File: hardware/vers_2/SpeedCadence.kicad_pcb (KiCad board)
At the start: 2 copper layers, 2 parts, among them IC1 AH1912-W-7, U2 STM32F103C8Tx

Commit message: PCB design complete
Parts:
- removed IC1: AH1912-W-7, Package_TO_SOT_SMD:SOT-23-3
- added C1: 100n, Capacitor_SMD:C_0805_2012Metric, F.Cu at (177.7, 107.2)
- added C10: 4.7n, Capacitor_SMD:C_0805_2012Metric, F.Cu at (157.8, 90.3)
- added C2: 100n, Capacitor_SMD:C_0805_2012Metric, F.Cu at (165.5, 104.2)
- added C3: 100n, Capacitor_SMD:C_0805_2012Metric, F.Cu at (167.7, 96.0)
- added C4: 100n, Capacitor_SMD:C_0805_2012Metric, F.Cu at (181.0, 96.3)
- added C5: 10u, Capacitor_SMD:C_0805_2012Metric, F.Cu at (174.6, 108.0)
- added C6: 100n, Capacitor_SMD:C_0805_2012Metric, F.Cu at (181.0, 98.6)
- added C7: 100n, Capacitor_SMD:C_0805_2012Metric, F.Cu at (165.5, 100.3)
- added C8: 1u, Capacitor_SMD:C_0805_2012Metric, F.Cu at (156.3, 103.2)
- added C9: 1u, Capacitor_SMD:C_0805_2012Metric, F.Cu at (163.2, 103.2)
- added D1: PTVS5V0Z1USK, Diode_SMD:Nexperia_DSN1608-2_1.6x0.8mm, F.Cu at (153.9, 111.1)
- added D2: D_Schottky, Diode_SMD:D_SOD-123, F.Cu at (156.3, 109.1)
- added D3: D_Schottky, Diode_SMD:D_SOD-123, F.Cu at (156.7, 98.3)
- added F1: Polyfuse, Fuse:Fuse_1206_3216Metric, F.Cu at (150.6, 111.1)
- added H1: MountingHole, MountingHole:MountingHole_2.2mm_M2, F.Cu at (187.4, 114.6)
- added H2: MountingHole, MountingHole:MountingHole_2.2mm_M2, F.Cu at (146.9, 114.6)
- added H3: MountingHole, MountingHole:MountingHole_2.2mm_M2, F.Cu at (187.4, 89.2)
- added H4: MountingHole, MountingHole:MountingHole_2.2mm_M2, F.Cu at (146.9, 89.2)
- added J1: Conn_ST_STDC14, Connector_PinHeader_1.27mm:PinHeader_2x07_P1.27mm_Vertical_SMD, F.Cu at (163.6, 111.6)
- added J2: USB_C_Receptacle_USB2.0_16P, Connector_USB:USB_C_Receptacle_HRO_TYPE-C-31-M-12, F.Cu at (149.4, 104.2)
- added J3: Conn_01x03_Pin, Connector_JST:JST_XH_B3B-XH-A_1x03_P2.50mm_Vertical, F.Cu at (176.1, 90.8)
- added J4: Conn_01x02_Pin, Connector_JST:JST_XH_B2B-XH-A_1x02_P2.50mm_Vertical, F.Cu at (167.4, 90.7)
- added J5: Conn_01x04_Pin, Connector_JST:JST_XH_B4B-XH-A_1x04_P2.50mm_Vertical, F.Cu at (173.1, 112.0)
- added J6: Conn_01x02_Pin, Connector_JST:JST_PH_B2B-PH-K_1x02_P2.00mm_Vertical, F.Cu at (147.4, 96.3)
- added R1: 5.1k, Resistor_SMD:R_0805_2012Metric, F.Cu at (153.1, 97.7)
- added R2: 5.1k, Resistor_SMD:R_0805_2012Metric, F.Cu at (153.0, 92.8)
- added R3: 60, Resistor_SMD:R_0805_2012Metric, F.Cu at (160.9, 91.0)
- added R4: 60, Resistor_SMD:R_0805_2012Metric, F.Cu at (160.9, 88.9)
- added R5: 4.7k, Resistor_SMD:R_0805_2012Metric, F.Cu at (182.6, 107.2)
- added R6: 4.7k, Resistor_SMD:R_0805_2012Metric, F.Cu at (184.9, 107.2)
- added SW2: SW_Push, Button_Switch_SMD:SW_SPST_SKQG_WithStem, F.Cu at (186.0, 99.6)
- added U1: AP2112K-3.3, Package_TO_SOT_SMD:SOT-23-5, F.Cu at (159.8, 103.2)
- added U3: TCAN3414DR, Package_SO:SOIC-8_3.9x4.9mm_P1.27mm, F.Cu at (161.2, 97.0)
- added Y1: CSTNE8M00G52Z000R0, OSC_CST:OSC_CSTNE8M00G52Z000R0, F.Cu at (180.5, 102.3)
- moved U2 104.2 mm to (173.2, 101.0), turned to 180 degrees
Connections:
- U2 pad 10: unconnected-(U2-PA0-Pad10) -> SENS_OUT
- U2 pad 18: unconnected-(U2-PB0-Pad18) -> STB
- U2 pad 19: unconnected-(U2-PB1-Pad19) -> SHDN
- U2 pad 32: unconnected-(U2-PA11-Pad32) -> CAN_RX
- U2 pad 33: unconnected-(U2-PA12-Pad33) -> CAN_TX
- U2 pad 42: unconnected-(U2-PB6-Pad42) -> OLED_SCL
- U2 pad 43: unconnected-(U2-PB7-Pad43) -> OLED_SDA
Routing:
- net +3.3V: track 0.00 -> 92.7 mm
- net PROG_RST: track 0.00 -> 33.1 mm, vias 0 -> 2
- net GND: track 0.00 -> 24.0 mm, vias 0 -> 24
- net CANL: track 0.00 -> 19.0 mm
- net OLED_SDA: track 0.00 -> 18.4 mm, vias 0 -> 1
- net OLED_SCL: track 0.00 -> 17.4 mm, vias 0 -> 1
- net STB: track 0.00 -> 17.4 mm, vias 0 -> 2
- net PROG_RX: track 0.00 -> 17.0 mm, vias 0 -> 2
- net Net-(F1-Pad2): track 0.00 -> 15.9 mm
- net Net-(J2-CC2): track 0.00 -> 15.2 mm, vias 0 -> 2
- net PROG_SWD: track 0.00 -> 15.0 mm, vias 0 -> 2
- net CAN_TX: track 0.00 -> 12.6 mm, vias 0 -> 2
- net +V_IN: track 0.00 -> 12.2 mm
- net SHDN: track 0.00 -> 11.2 mm, vias 0 -> 2
- net SENS_OUT: track 0.00 -> 10.5 mm, vias 0 -> 1
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- added copper zone on B.Cu, net GND
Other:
- board outline added: 46 x 31 mm
- board text added: "2.769mm"

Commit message: Small adjustment
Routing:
- net +3.3V: track 92.7 -> 93.9 mm
- net Net-(F1-Pad2): track 15.9 -> 16.8 mm

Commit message: Fixed minor changes
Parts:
- added R8: 10k, Resistor_SMD:R_0805_2012Metric, F.Cu at (180.4, 107.3)
- added SW3: SW_Push, Button_Switch_SMD:SW_SPST_SKQG_WithStem, F.Cu at (187.3, 103.7)
- moved R6 4.64 mm to (189.2, 108.8)
- moved R5 3.06 mm to (185.2, 108.8)
- moved SW2 2.46 mm to (187.4, 97.6), turned to 0 degrees
- moved H1 2.02 mm to (189.4, 114.6)
- moved H3 2.02 mm to (189.4, 89.2)
- moved J2 1.12 mm to (148.3, 104.3)
- moved J3 0.69 mm to (176.1, 90.1)
- moved J5 0.69 mm to (173.1, 112.7)
- moved C8 0.66 mm to (155.7, 103.1)
- moved J1 0.64 mm to (163.6, 112.3)
- moved J4 0.62 mm to (167.4, 90.1)
- moved U1 0.41 mm to (159.4, 103.1)
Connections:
- J6 pad 1: +V_BATT -> GND
- J6 pad 2: GND -> +V_BATT
- U2 pad 10: SENS_OUT -> unconnected-(U2-PA0-Pad10)
- U2 pad 11: unconnected-(U2-PA1-Pad11) -> SENS_OUT
- U2 pad 44: GND -> Net-(U2-BOOT0)
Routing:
- net Net-(U2-BOOT0): track 0.00 -> 24.8 mm, vias 0 -> 3
- net +3.3V: track 93.9 -> 106.3 mm
- net OLED_SDA: track 18.4 -> 25.0 mm
- net GND: track 24.0 -> 21.3 mm, vias 24 -> 25
- net PROG_RX: track 17.0 -> 18.2 mm
- net OLED_SCL: track 17.4 -> 18.5 mm
- net +V_BATT: track 9.40 -> 10.4 mm
- net Net-(F1-Pad2): track 16.8 -> 15.9 mm
- net PROG_TX: track 10.1 -> 10.8 mm
- net PROG_SWD: track 15.0 -> 15.7 mm
- net PROG_CLK: track 10.4 -> 11.1 mm
- net Net-(J2-CC1): track 7.53 -> 8.16 mm
- net PROG_RST: track 33.1 -> 32.5 mm
- net CANL: track 19.0 -> 19.5 mm
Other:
- board size 46 x 31 mm -> 48 x 31 mm

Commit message: removed tvs diode
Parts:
- removed D1: PTVS5V0Z1USK, Diode_SMD:Nexperia_DSN1608-2_1.6x0.8mm
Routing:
- net GND: track 21.3 -> 20.6 mm, vias 25 -> 24

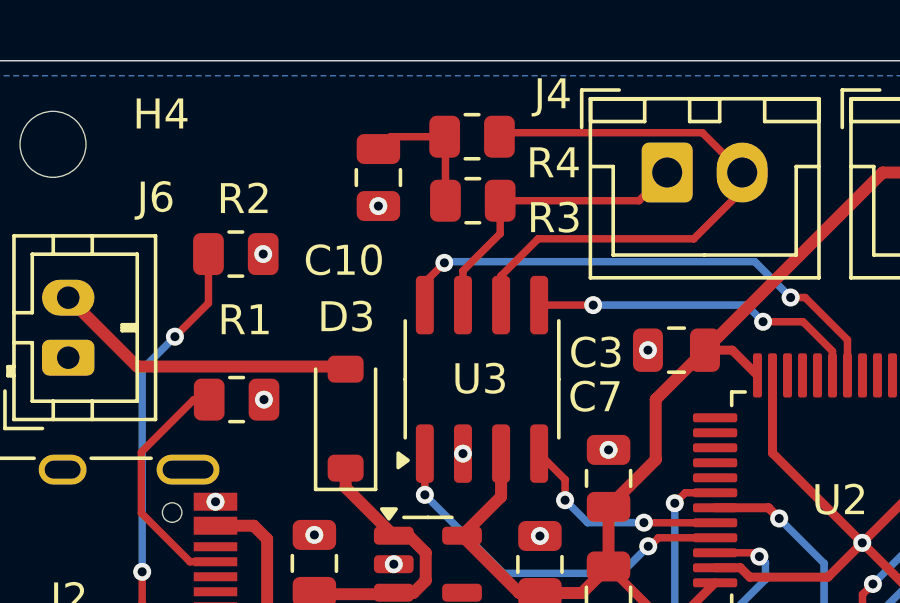
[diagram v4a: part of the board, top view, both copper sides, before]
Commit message: R3, R4 changed to 0603 footprint
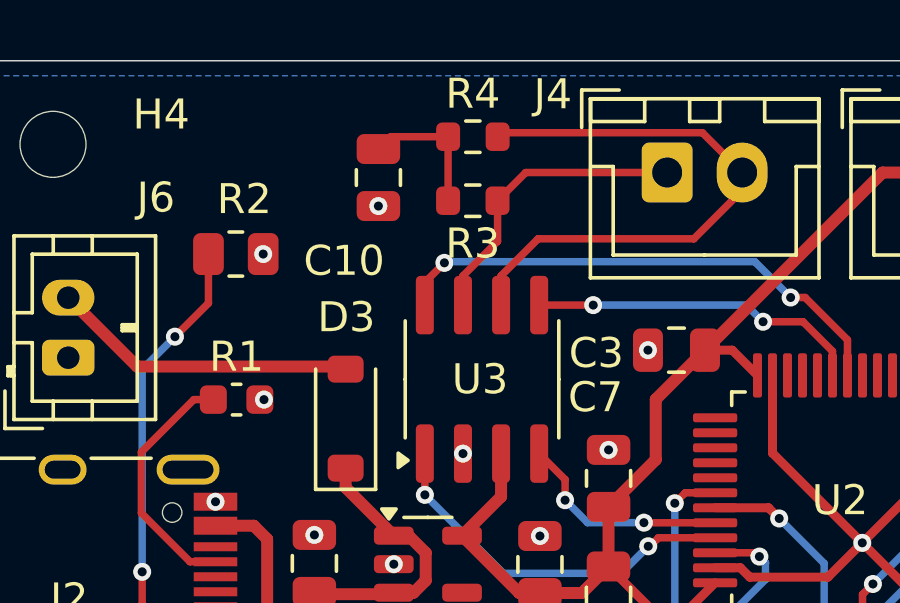
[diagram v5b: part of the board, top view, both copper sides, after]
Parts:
- R1: footprint Resistor_SMD:R_0805_2012Metric -> Capacitor_SMD:C_0603_1608Metric
- R3, R4: footprint Resistor_SMD:R_0805_2012Metric -> Resistor_SMD:R_0603_1608Metric

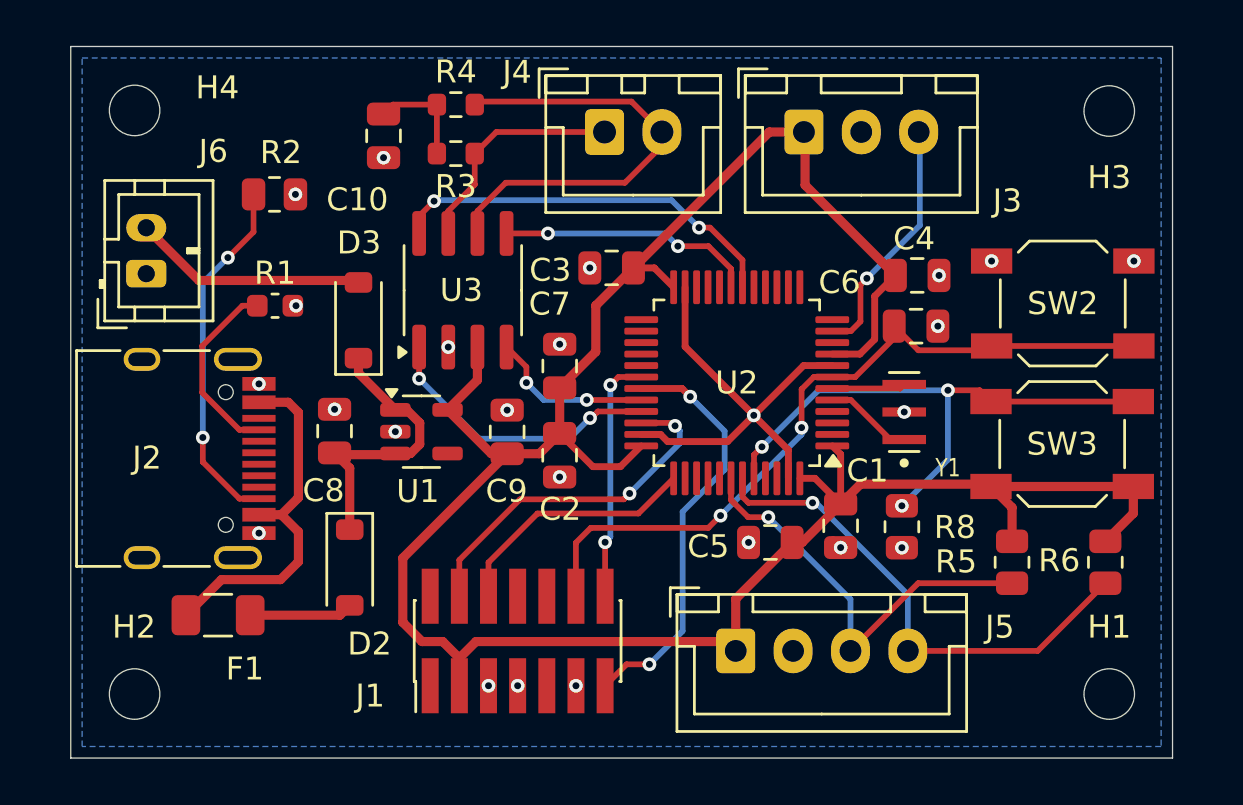
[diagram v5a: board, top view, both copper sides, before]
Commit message: Changed to 6.4V with buck converter
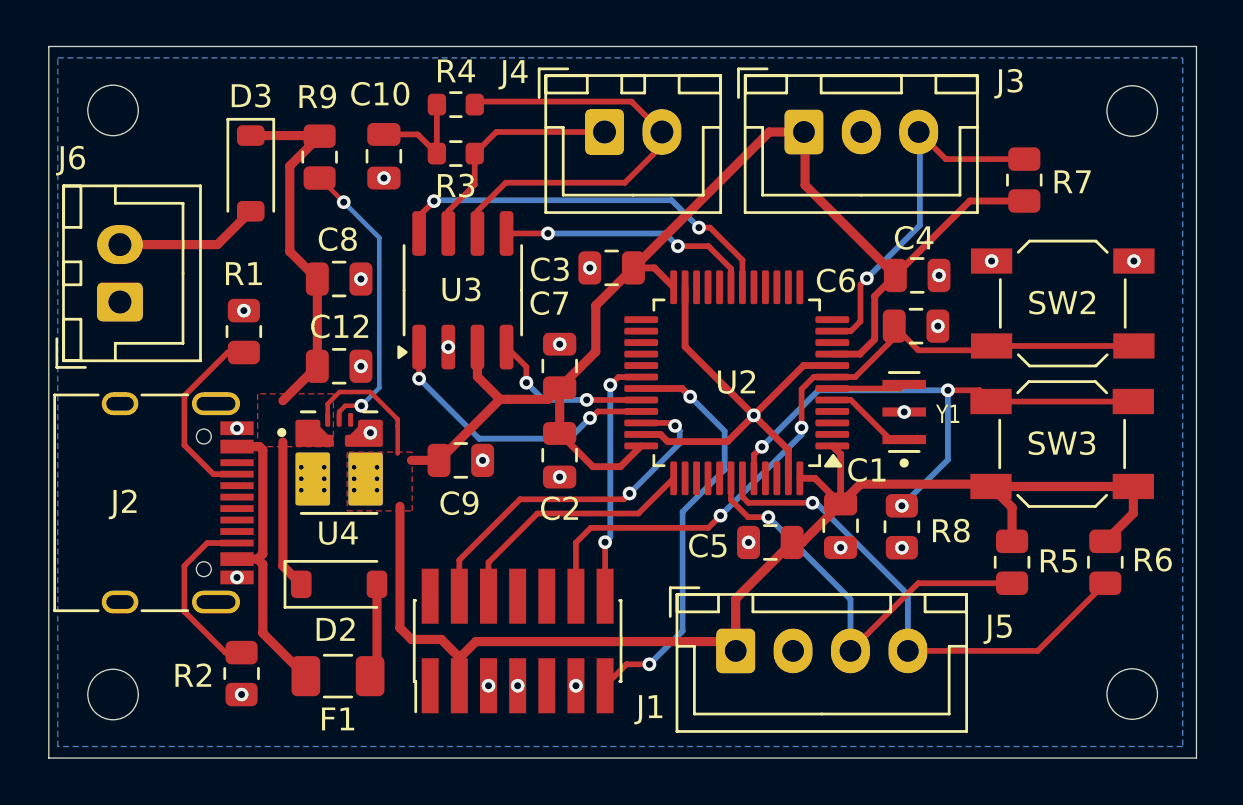
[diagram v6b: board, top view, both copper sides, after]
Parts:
- removed U1: AP2112K-3.3, Package_TO_SOT_SMD:SOT-23-5
- added C12: 10u, Capacitor_SMD:C_0805_2012Metric, F.Cu at (155.8, 100.3)
- added R7: 4.7k, Resistor_SMD:R_0805_2012Metric, F.Cu at (185.7, 92.2)
- added R9: 2.7M, Resistor_SMD:R_0805_2012Metric, F.Cu at (155.0, 91.2)
- added U4: TPSM861253RDXR, TPSM861253:VREG_TPSM861253RDXR, F.Cu at (155.8, 104.5)
- C8: value 1u -> 100n
- C9: value 1u -> 22u
- J6: footprint Connector_JST:JST_PH_B2B-PH-K_1x02_P2.00mm_Vertical -> Connector_JST:JST_XH_B2B-XH-A_1x02_P2.50mm_Vertical
- R1: footprint Capacitor_SMD:C_0603_1608Metric -> Resistor_SMD:R_0805_2012Metric
- moved R2 20.9 mm to (151.6, 113.7), turned to -90 degrees
- moved D3 7.93 mm to (152.0, 91.9), turned to -90 degrees
- moved C8 6.63 mm to (155.8, 96.5), turned to 0 degrees
- moved F1 5.86 mm to (155.8, 113.8)
- moved C9 2.37 mm to (161.2, 104.4), turned to 0 degrees
- moved J2 2.16 mm to (147.4, 106.2)
- moved R1 1.76 mm to (151.7, 98.8), turned to 90 degrees
- moved J6 1.68 mm to (146.3, 97.5)
- moved H1 1.00 mm to (190.4, 114.6)
- moved H3 1.00 mm to (190.4, 89.2)
- moved H2 0.94 mm to (146.0, 114.6)
- moved H4 0.94 mm to (146.0, 89.2)
- moved C10 0.89 mm to (157.8, 91.2)
- moved D2 0.87 mm to (155.8, 109.8), turned to 0 degrees
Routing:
- net Net-(U4-EN): track 0.00 -> 12.7 mm, vias 0 -> 2
- net +V_IN: track 12.7 -> 22.7 mm
- net +3.3V: track 106.3 -> 116.0 mm
- net Net-(J2-CC2): track 15.7 -> 7.93 mm, vias 2 -> 0
- net SENS_OUT: track 10.7 -> 15.8 mm
- net +V_BATT: track 10.4 -> 6.30 mm
- net Net-(F1-Pad2): track 15.9 -> 12.9 mm
- net GND: vias 24 -> 25
- added copper zone on F.Cu, net +3.3V
- added copper zone on F.Cu, net +V_IN
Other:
- board size 48 x 31 mm -> 50 x 31 mm
- board text added: "Speed and Cadence V2"

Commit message: minor changes
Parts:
- renumbered C12 to C11
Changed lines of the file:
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@@
 		(descr "Capacitor SMD 0805 (2012 Metric), square (rectangular) end terminal, IPC_7351 nominal, (Body size source: IPC-SM-782 page 76, https://www.pcb-3d.com/wordpress/wp-content/uploads/ipc-sm-782a_amendment_1_and_2.pdf, https://docs.google.com/spreadsheets/d/1BsfQQcO9C6DZCsRaXUlFlo91Tg2WpOkGARC1WS5S8t0/edit?usp=sharing), generated with kicad-footprint-generator")
 		(tags "capacitor")
-		(property "Reference" "C12"
+		(property "Reference" "C11"
 			(at 0.05 -1.7 0)
 			(layer "F.SilkS")

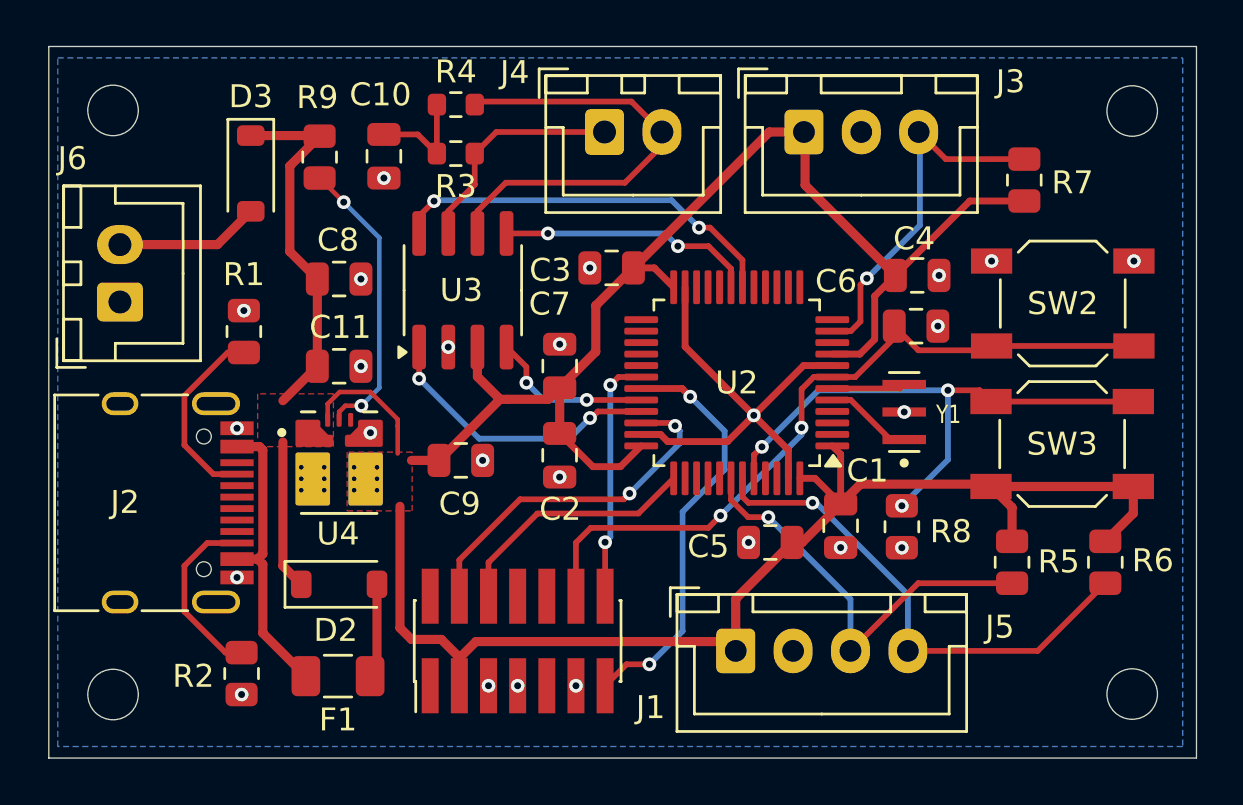
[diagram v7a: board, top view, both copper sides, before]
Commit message: test LED and USB footprint change
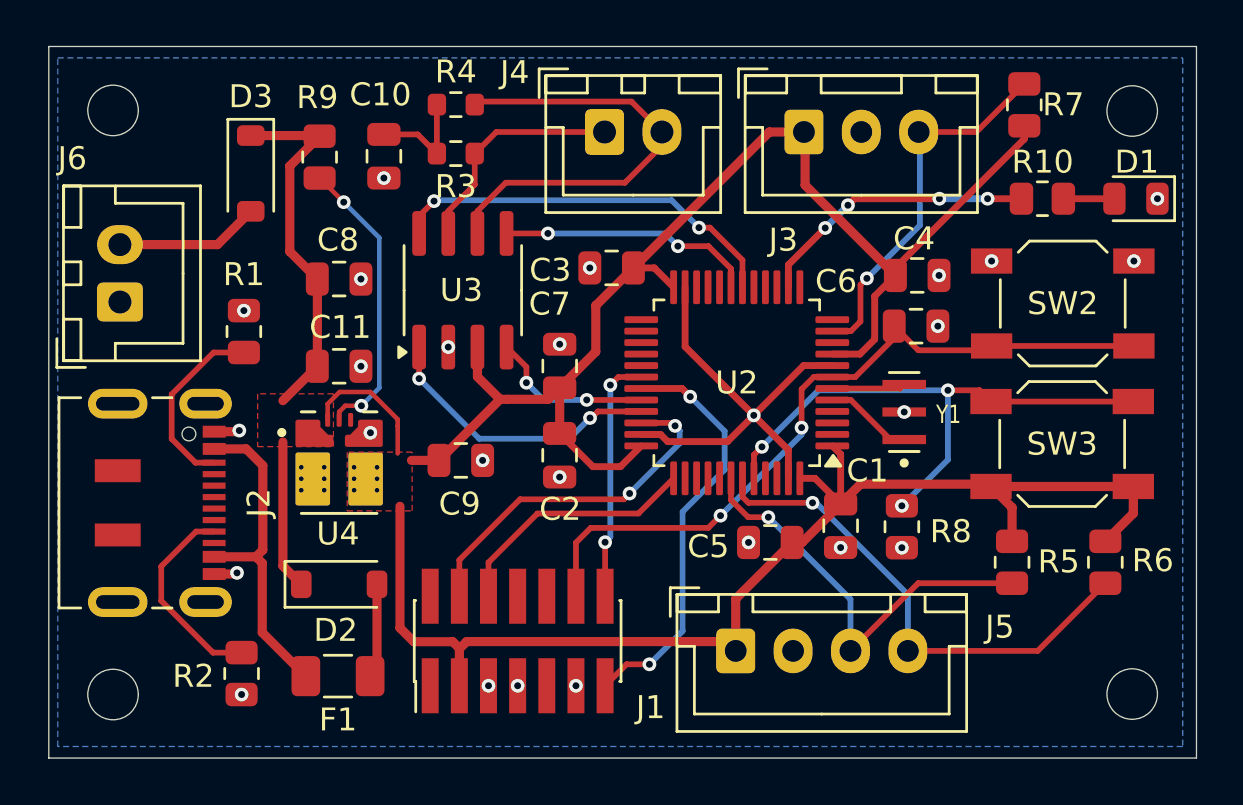
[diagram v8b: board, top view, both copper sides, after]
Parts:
- added D1: LED, LED_SMD:LED_0805_2012Metric, F.Cu at (190.6, 93.0)
- added R10: 330, Resistor_SMD:R_0805_2012Metric, F.Cu at (186.5, 93.0)
- J2: footprint Connector_USB:USB_C_Receptacle_HRO_TYPE-C-31-M-12 -> Connector_USB:USB_C_Receptacle_JAE_DX07S016JA1R1500
- moved R7 3.28 mm to (185.7, 88.9)
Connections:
- U2 pad 14: unconnected-(U2-PA4-Pad14) -> TEST_LED
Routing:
- net TEST_LED: track 0.00 -> 12.3 mm, vias 0 -> 4
- net Net-(D1-A): track 0.00 -> 2.22 mm
- net GND: track 20.6 -> 22.7 mm, vias 25 -> 26
- net +3.3V: track 116.0 -> 118.0 mm
- net Net-(F1-Pad2): track 12.9 -> 14.4 mm
- net Net-(J2-CC2): track 7.93 -> 8.87 mm
